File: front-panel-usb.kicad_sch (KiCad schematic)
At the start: 89 parts, among them J10 USB-C_Kycon_KUSBX-SL2-CS1N24-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, J11 USB-C_Kycon_KUSBX-SL2-CS1N24-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, J9 USB-C_Kycon_KUSBX-SL2-CS1N24-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, Q9 PJE138K, U26 AP22615B_TSOT26, U27 FUSB303B, U28 TPD4E05U06QDQARQ1, U29 TPD4E05U06QDQARQ1, U30 AP22615B_TSOT26, U31 HD3SS3220RNH, U32 TPD4E05U06QDQARQ1, U33 74LVC06ABQ, U34 TPD4E05U06QDQARQ1, U35 TPD4E05U06QDQARQ1, U36 74AUP2G132

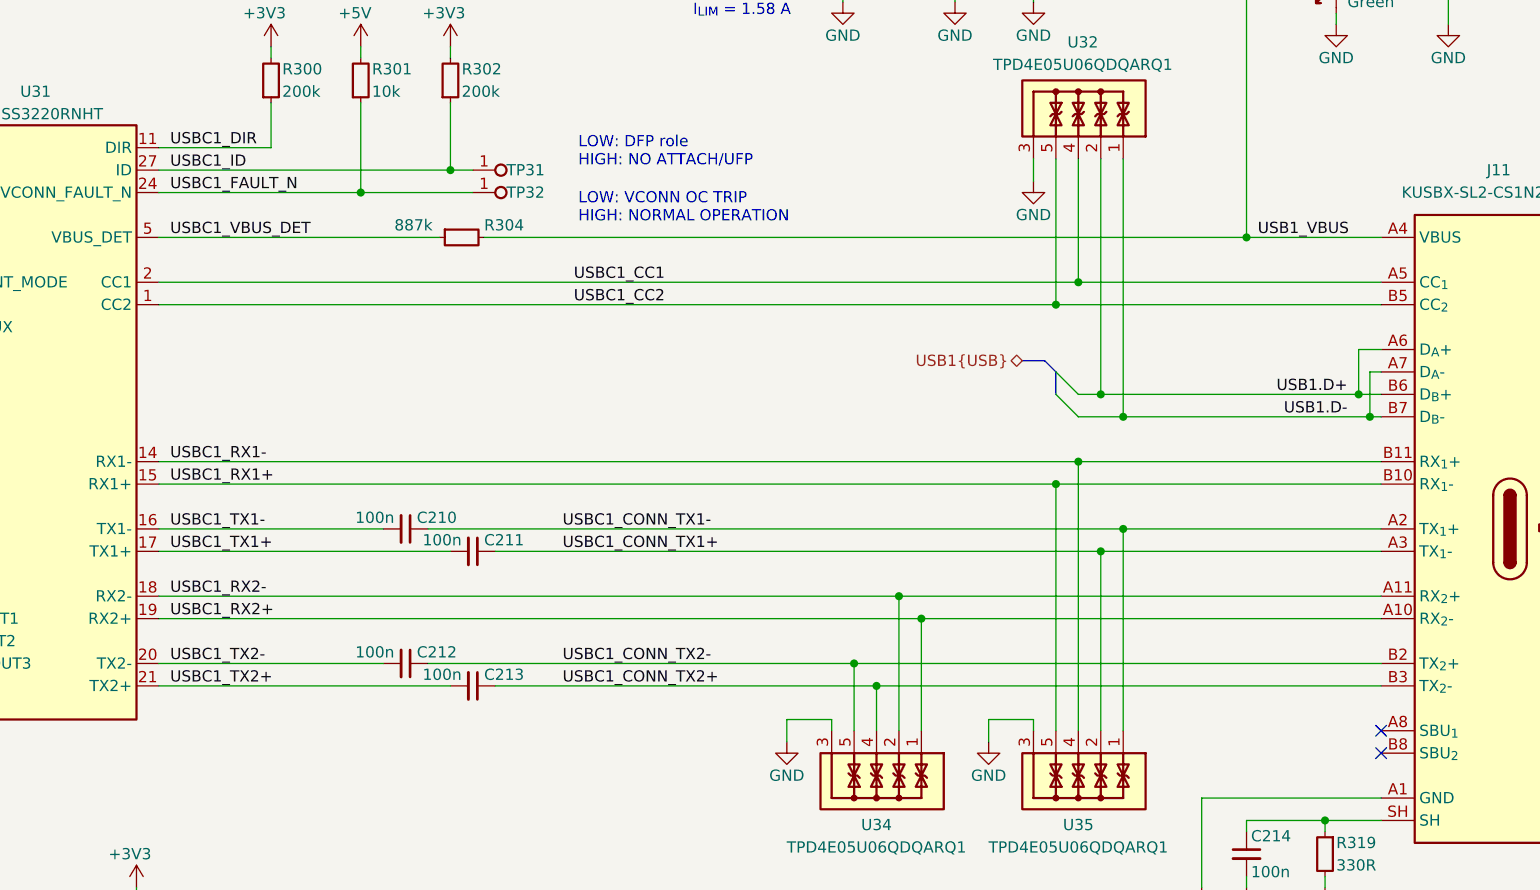
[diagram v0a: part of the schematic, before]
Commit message: [#100707] Finish rerouting front panel USB
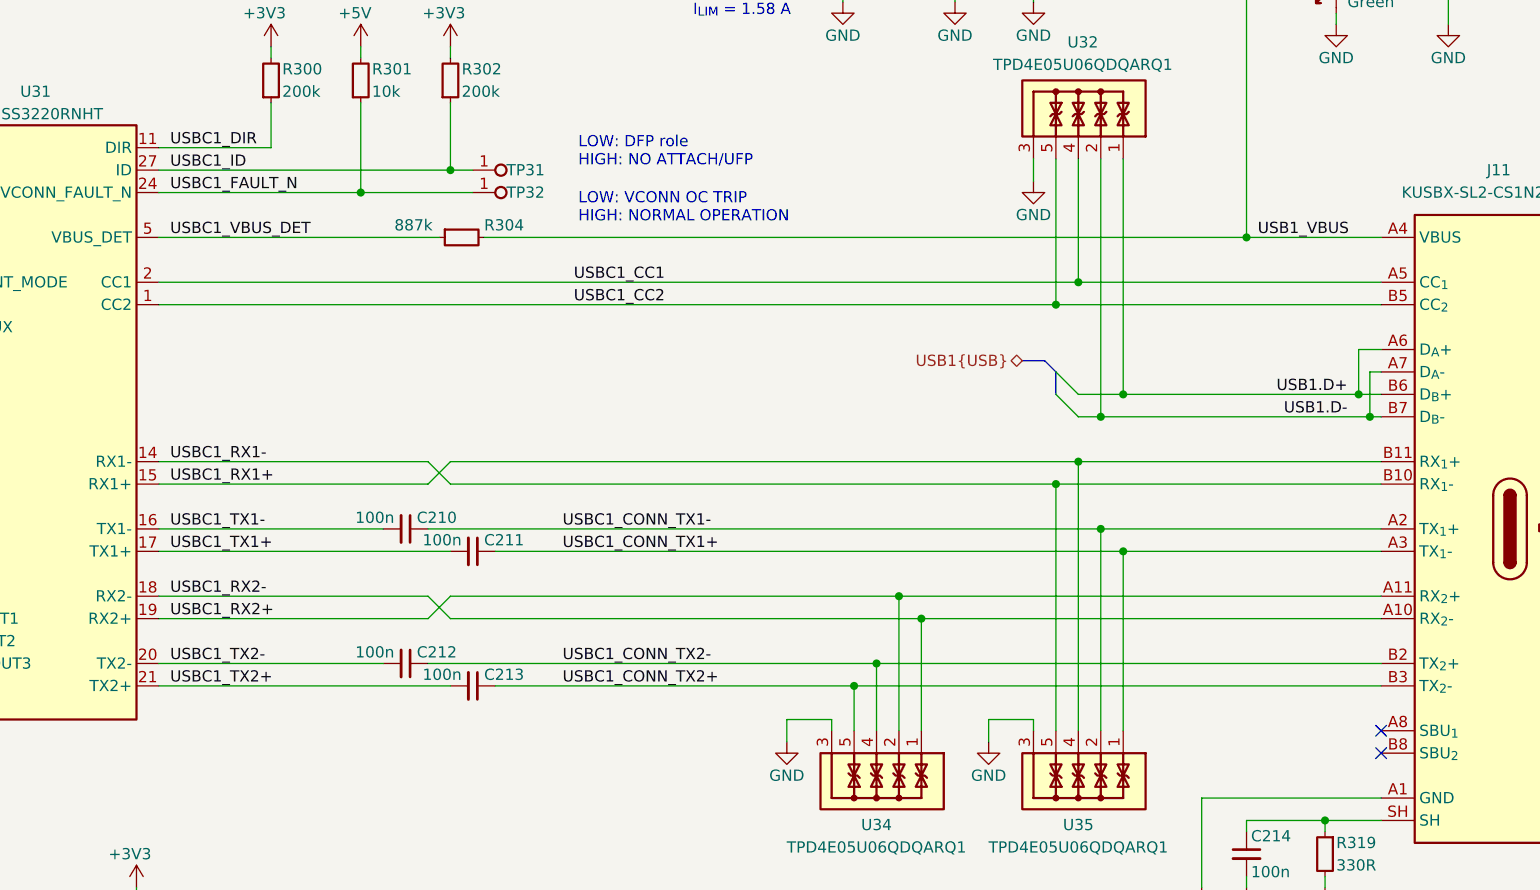
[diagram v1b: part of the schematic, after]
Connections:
- net USB1.D+: now also U32.1, U32.10; no longer U32.2, U32.9
- net USB1.D-: now also U32.2, U32.9; no longer U32.1, U32.10
- net USBC1_CONN_TX1+: now also U35.1, U35.10; no longer U35.2, U35.9
- net USBC1_CONN_TX1-: now also U35.2, U35.9; no longer U35.1, U35.10
- net USBC1_CONN_TX2+: now also U34.5, U34.6; no longer U34.4, U34.7
- net USBC1_CONN_TX2-: now also U34.4, U34.7; no longer U34.5, U34.6
- net USBC1_RX1+: now also J11.B11 (RX_{1}+), U35.4, U35.7; no longer J11.B10 (RX_{1}-), U35.5, U35.6
- net USBC1_RX1-: now also J11.B10 (RX_{1}-), U35.5, U35.6; no longer J11.B11 (RX_{1}+), U35.4, U35.7
- net USBC1_RX2+: now also J11.A11 (RX_{2}+), U34.2, U34.9; no longer J11.A10 (RX_{2}-), U34.1, U34.10
- net USBC1_RX2-: now also J11.A10 (RX_{2}-), U34.1, U34.10; no longer J11.A11 (RX_{2}+), U34.2, U34.9

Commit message: [#101340] Update USB ILIM resistors to 4k7
Re-use 4k7 resistors from other sheets. Resulting current ~1.45A
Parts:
- R283, R299: value R_4k3_0402 -> R_4k7_0402; symbol antmicroResistors0402:R_4k3_0402 -> antmicroResistors0402:R_4k7_0402; MPN RMCF0402FT4K30 -> CR0402-FX-4701GLF; Manufacturer Stackpole Electronics -> Bourns; Val 4k3 -> 4k7
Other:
- note added: "I_{LIM} = 6800/R I_{LIM} = 1.45 A"
- note removed: "I_{LIM} = 6800/R I_{LIM} = 1.58 A"
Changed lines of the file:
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@@
 		)
 	)
-	(text "I_{LIM} = 6800/R\nI_{LIM} = 1.58 A"
+	(text "I_{LIM} = 6800/R\nI_{LIM} = 1.45 A"
 		(exclude_from_sim no)
 		(at 279.4 38.1 0)
@@
 		)
 	)
-	(text "I_{LIM} = 6800/R\nI_{LIM} = 1.58 A"
+	(text "I_{LIM} = 6800/R\nI_{LIM} = 1.45 A"
 		(exclude_from_sim no)
 		(at 306.07 144.78 0)
@@
 	)
 	(symbol
-		(lib_id "antmicroResistors0402:R_4k3_0402")
+		(lib_id "antmicroResistors0402:R_4k7_0402")
 		(at 290.83 35.56 90)
 		(unit 1)
@@
 			)
 		)
-		(property "Value" "R_4k3_0402"
+		(property "Value" "R_4k7_0402"
 			(at 303.53 15.24 0)
 			(hide yes)
@@
 			)
 		)
-		(property "Datasheet" "https://www.farnell.com/datasheets/3795017.pdf"
+		(property "Datasheet" "https://www.bourns.com/docs/product-datasheets/cr.pdf"
 			(at 308.61 15.24 0)
 			(hide yes)
@@
 			)
 		)
-		(property "Description" "SMD Chip Resistor, 3.24 kohm, ± 1%, 62.5 mW, 0402 [1005 Metric], Thick Film, General Purpose"
+		(property "Description" "SMD Chip Resistor, 4.7 kohm, ± 1%, 62.5 mW, 0402 [1005 Metric], Thick Film, General Purpose"
 			(at 321.31 15.24 0)
 			(hide yes)
@@
 			)
 		)
-		(property "MPN" "RMCF0402FT4K30"
+		(property "MPN" "CR0402-FX-4701GLF"
 			(at 311.15 15.24 0)
 			(hide yes)
@@
 			)
 		)
-		(property "Manufacturer" "Stackpole Electronics"
+		(property "Manufacturer" "Bourns"
 			(at 313.69 15.24 0)
 			(hide yes)
@@
 			)
 		)
-		(property "Val" "4k3"
+		(property "Val" "4k7"
 			(at 292.1 34.29 90)
 			(show_name no)
@@
 	)
 	(symbol
-		(lib_id "antmicroResistors0402:R_4k3_0402")
+		(lib_id "antmicroResistors0402:R_4k7_0402")
 		(at 317.5 142.24 90)
 		(unit 1)
@@
 			)
 		)
-		(property "Value" "R_4k3_0402"
+		(property "Value" "R_4k7_0402"
 			(at 330.2 121.92 0)
 			(hide yes)
@@
 			)
 		)
-		(property "Datasheet" "https://www.farnell.com/datasheets/3795017.pdf"
+		(property "Datasheet" "https://www.bourns.com/docs/product-datasheets/cr.pdf"
 			(at 335.28 121.92 0)
 			(hide yes)
@@
 			)
 		)
-		(property "Description" "SMD Chip Resistor, 3.24 kohm, ± 1%, 62.5 mW, 0402 [1005 Metric], Thick Film, General Purpose"
+		(property "Description" "SMD Chip Resistor, 4.7 kohm, ± 1%, 62.5 mW, 0402 [1005 Metric], Thick Film, General Purpose"
 			(at 347.98 121.92 0)
 			(hide yes)
@@
 			)
 		)
-		(property "MPN" "RMCF0402FT4K30"
+		(property "MPN" "CR0402-FX-4701GLF"
 			(at 337.82 121.92 0)
 			(hide yes)
@@
 			)
 		)
-		(property "Manufacturer" "Stackpole Electronics"
+		(property "Manufacturer" "Bourns"
 			(at 340.36 121.92 0)
 			(hide yes)
@@
 			)
 		)
-		(property "Val" "4k3"
+		(property "Val" "4k7"
 			(at 318.77 140.97 90)
 			(show_name no)

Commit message: [#101340] Unify LEDs resistor values
Front panel resistors @ 330Ohm, remaining ones 1kOhm
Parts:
- R290, R298: value R_330R_0402 -> R_1k_0402; symbol antmicroResistors0402:R_330R_0402 -> antmicroResistors0402:R_1k_0402; MPN CR0402-FX-3300GLF -> CR0402-FX-1001GLF; Val 330R -> 1k
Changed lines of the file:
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@@
 	)
 	(symbol
-		(lib_id "antmicroResistors0402:R_330R_0402")
+		(lib_id "antmicroResistors0402:R_1k_0402")
 		(at 341.63 81.28 270)
 		(mirror x)
@@
 		(dnp no)
 		(property "Reference" "R290"
-			(at 342.9 77.47 90)
+			(at 343.154 77.47 90)
 			(show_name no)
 			(do_not_autoplace no)
@@
 			)
 		)
-		(property "Value" "R_330R_0402"
+		(property "Value" "R_1k_0402"
 			(at 328.93 60.96 0)
 			(hide yes)
@@
 			)
 		)
-		(property "Description" "SMD Chip Resistor, 330 ohm, ± 1%, 62.5 mW, 0402 [1005 Metric], Thick Film, General Purpose"
+		(property "Description" "SMD Chip Resistor, 1 kohm, ± 1%, 63 mW, 0402 [1005 Metric], Thick Film, General Purpose"
 			(at 341.63 81.28 0)
 			(hide yes)
@@
 					(size 1.27 1.27)
 				)
+				(justify left bottom)
 			)
 		)
-		(property "MPN" "CR0402-FX-3300GLF"
+		(property "MPN" "CR0402-FX-1001GLF"
 			(at 321.31 60.96 0)
 			(hide yes)
@@
 			)
 		)
-		(property "Val" "330R"
-			(at 342.9 80.01 90)
+		(property "Val" "1k"
+			(at 343.154 80.01 90)
 			(show_name no)
 			(do_not_autoplace no)
@@
 	)
 	(symbol
-		(lib_id "antmicroResistors0402:R_330R_0402")
+		(lib_id "antmicroResistors0402:R_1k_0402")
 		(at 373.38 139.7 270)
 		(mirror x)
@@
 			)
 		)
-		(property "Value" "R_330R_0402"
+		(property "Value" "R_1k_0402"
 			(at 360.68 119.38 0)
 			(hide yes)
@@
 			)
 		)
-		(property "Description" "SMD Chip Resistor, 330 ohm, ± 1%, 62.5 mW, 0402 [1005 Metric], Thick Film, General Purpose"
+		(property "Description" "SMD Chip Resistor, 1 kohm, ± 1%, 63 mW, 0402 [1005 Metric], Thick Film, General Purpose"
 			(at 373.38 139.7 0)
 			(hide yes)
@@
 			)
 		)
-		(property "MPN" "CR0402-FX-3300GLF"
+		(property "MPN" "CR0402-FX-1001GLF"
 			(at 353.06 119.38 0)
 			(hide yes)
@@
 			)
 		)
-		(property "Val" "330R"
+		(property "Val" "1k"
 			(at 374.65 138.43 90)
 			(show_name no)

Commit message: [#101340] Reduce number of unique R MPNs
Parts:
- R289, R293: value R_910k_0402 -> R_887k_0402; symbol antmicroResistors0402:R_910k_0402 -> antmicroResistors0402:R_887k_0402; MPN CR0402-FX-9103GLF -> ERJ-2RKF8873X; Manufacturer Bourns -> Panasonic; Val 910k -> 887k
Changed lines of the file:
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@@
 	)
 	(symbol
-		(lib_id "antmicroResistors0402:R_910k_0402")
+		(lib_id "antmicroResistors0402:R_887k_0402")
 		(at 254 78.74 90)
 		(unit 1)
@@
 			)
 		)
-		(property "Value" "R_910k_0402"
+		(property "Value" "R_887k_0402"
 			(at 266.7 58.42 0)
 			(hide yes)
@@
 			)
 		)
-		(property "Datasheet" "https://www.bourns.com/docs/product-datasheets/cr.pdf"
+		(property "Datasheet" "https://eu.mouser.com/datasheet/2/315/AOA0000C304-1149620.pdf"
 			(at 271.78 58.42 0)
 			(hide yes)
@@
 			)
 		)
-		(property "MPN" "CR0402-FX-9103GLF"
+		(property "MPN" "ERJ-2RKF8873X"
 			(at 274.32 58.42 0)
 			(hide yes)
@@
 			)
 		)
-		(property "Manufacturer" "Bourns"
+		(property "Manufacturer" "Panasonic"
 			(at 276.86 58.42 0)
 			(hide yes)
@@
 			)
 		)
-		(property "Val" "910k"
+		(property "Val" "887k"
 			(at 252.73 77.47 90)
 			(show_name no)
@@
 	)
 	(symbol
-		(lib_id "antmicroResistors0402:R_910k_0402")
+		(lib_id "antmicroResistors0402:R_887k_0402")
 		(at 254 92.71 90)
 		(mirror x)
@@
 			)
 		)
-		(property "Value" "R_910k_0402"
+		(property "Value" "R_887k_0402"
 			(at 266.7 113.03 0)
 			(hide yes)
@@
 			)
 		)
-		(property "Datasheet" "https://www.bourns.com/docs/product-datasheets/cr.pdf"
+		(property "Datasheet" "https://eu.mouser.com/datasheet/2/315/AOA0000C304-1149620.pdf"
 			(at 271.78 113.03 0)
 			(hide yes)
@@
 			)
 		)
-		(property "MPN" "CR0402-FX-9103GLF"
+		(property "MPN" "ERJ-2RKF8873X"
 			(at 274.32 113.03 0)
 			(hide yes)
@@
 			)
 		)
-		(property "Manufacturer" "Bourns"
+		(property "Manufacturer" "Panasonic"
 			(at 276.86 113.03 0)
 			(hide yes)
@@
 			)
 		)
-		(property "Val" "910k"
+		(property "Val" "887k"
 			(at 252.73 96.52 90)
 			(show_name no)
